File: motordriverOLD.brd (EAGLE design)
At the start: 101.3 x 82.5 mm, 99 parts, among them J1 CONNECTOR_MOTORS, J10 HEADER_1X3, J11 HEADER_1X3, J2 CONNECTOR_MOTORS, J3 CONNECTOR_MOTORS, J4 CONNECTOR_MOTORS, J5 HEADER_1X3, J6 HEADER_1X3, J7 HEADER_1X3, J8 HEADER_1X3, J9 CONNECTOR_MOTORS, Q1 MOSFET, Q10 MOSFET, Q11 MOSFET, Q12 MOSFET, Q13 MOSFET, Q14 MOSFET, Q15 MOSFET, Q16 MOSFET, Q2 MOSFET, Q3 MOSFET, Q4 MOSFET, Q5 MOSFET, Q6 MOSFET, Q7 MOSFET, Q8 MOSFET, Q9 MOSFET, U1 74XX139_PDIP, U10 IR2111_PDIP, U11 IR2111_PDIP, U12 7812_TO220, U2 TL084_PDIP, U3 7812_TO220, U4 IR2111_PDIP, U5 IR2111_PDIP, U6 IR2111_PDIP, U7 IR2111_PDIP, U8 IR2111_PDIP, U9 IR2111_PDIP

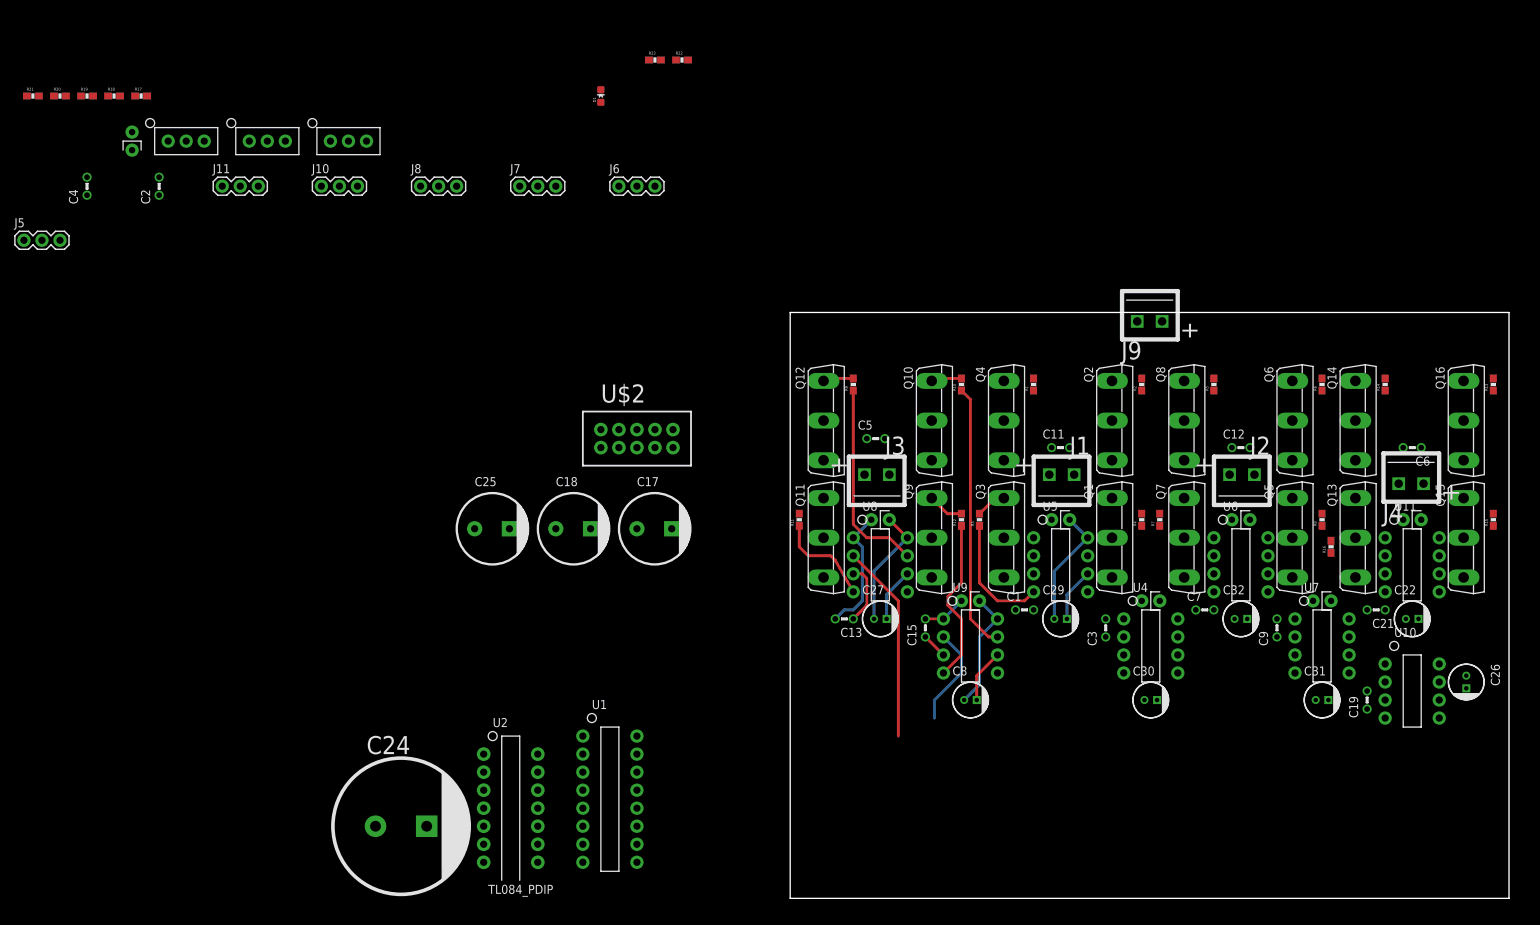
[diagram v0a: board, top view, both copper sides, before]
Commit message: PCB Layout Overhaul
Reworked H-Bridge, this time it will be possible to route VCC(24v)
without killing yourself.
Couple clearance issues that need to be cleared before I proceed.
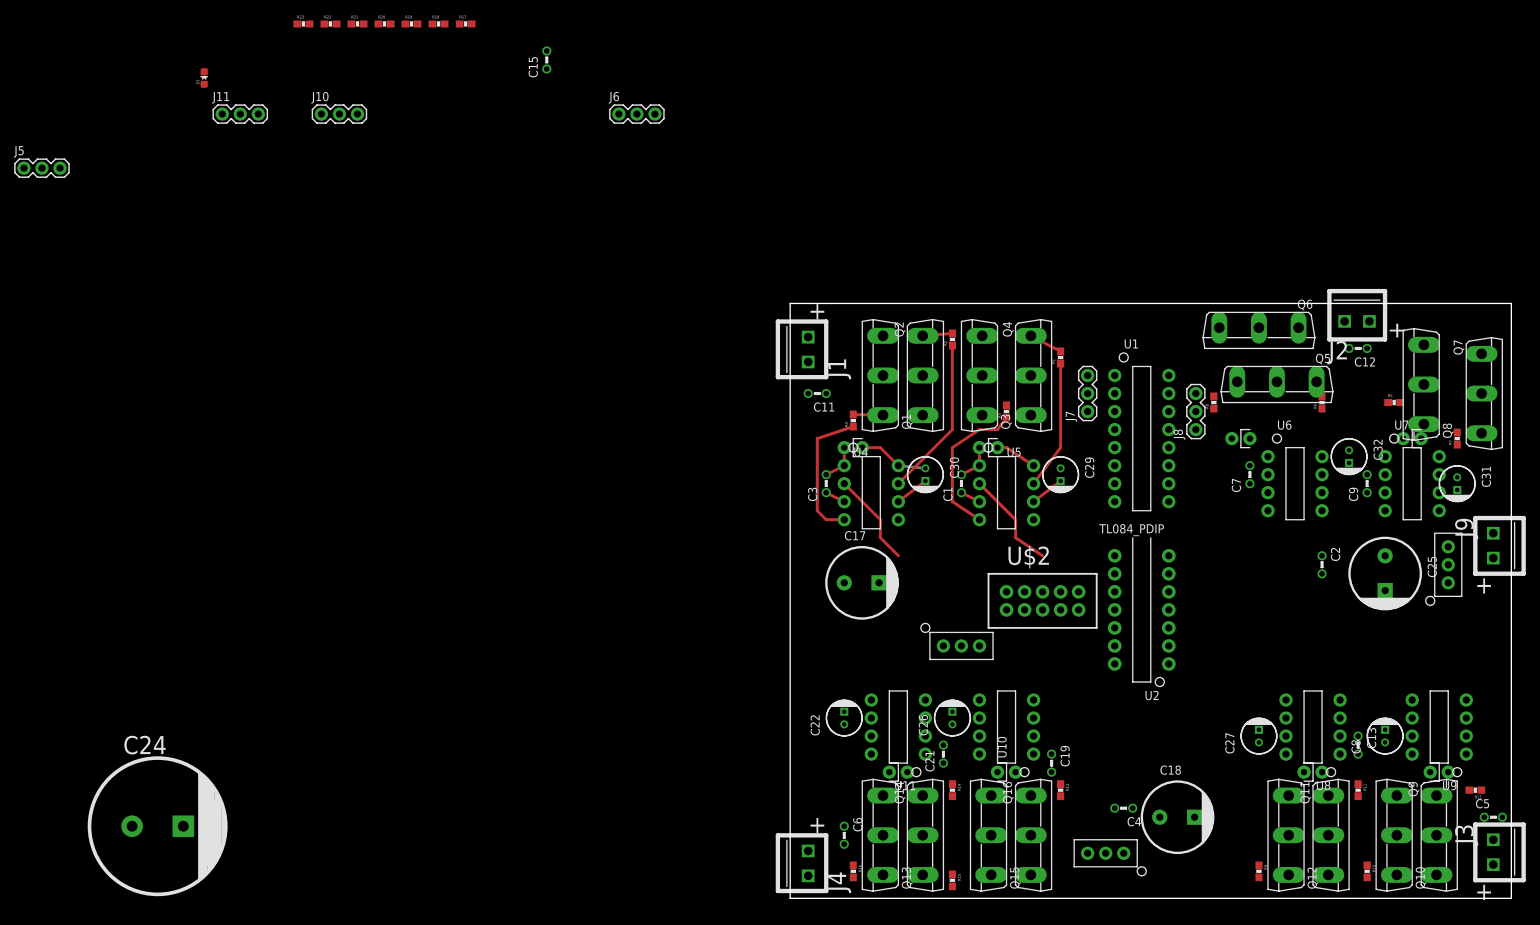
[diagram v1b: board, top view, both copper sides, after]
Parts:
- moved U3 176.8 mm to (92.7, 47.0), turned to 90 degrees
- moved C2 171.5 mm to (74.9, 48.3), turned to 180 degrees
- moved C4 170.8 mm to (48.3, 12.7), turned to 90 degrees
- moved D7 153.7 mm to (31.8, 17.8), turned to 270 degrees
- moved U$1 146.4 mm to (44.5, 6.35), turned to 180 degrees
- moved U12 130.3 mm to (24.1, 35.6)
- moved C25 128.3 mm to (83.8, 48.3), turned to 270 degrees
- moved J8 111.3 mm to (57.1, 68.6), turned to 90 degrees
- moved C5 102.0 mm to (97.8, 11.4)
- moved J3 102.0 mm to (99.1, 6.35), turned to 180 degrees
- moved J4 100.4 mm to (2.54, 5.08), turned to 0 degrees
- moved U2 97.4 mm to (53.3, 33.0), turned to 180 degrees
- moved C6 97.2 mm to (7.62, 10.2), turned to 180 degrees
- moved C15 96.2 mm to (-34.3, 116.8)
- moved C18 94.3 mm to (52.1, 11.4)
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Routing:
- net N$3: track 37.6 -> 0.00 mm
- net N$28: track 28.3 -> 0.00 mm
- net X_PWM_B: track 28.0 -> 0.00 mm
- net N$1: track 23.4 -> 0.00 mm
- net N$27: track 0.00 -> 22.6 mm
- net N$19: track 0.00 -> 19.8 mm
- net N$16: track 0.00 -> 18.2 mm
- net N$47: track 17.0 -> 0.00 mm
- net N$55: track 17.0 -> 0.00 mm
- net Y_PWM_B: track 0.00 -> 14.3 mm
- net X_PWM_A: track 14.1 -> 0.00 mm
- net N$29: track 13.9 -> 0.00 mm
- net Y_PWM_A: track 0.00 -> 13.3 mm
- net VCC_12V: track 24.0 -> 10.8 mm
- net N$13: track 17.0 -> 5.85 mm
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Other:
- board size 101.3 x 82.5 mm -> 101.6 x 83.8 mm
